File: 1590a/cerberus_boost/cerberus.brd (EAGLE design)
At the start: 33 x 31.7 mm, 30 parts, among them Q1 2N5088, Q2 2N5088, Q3 2N5087

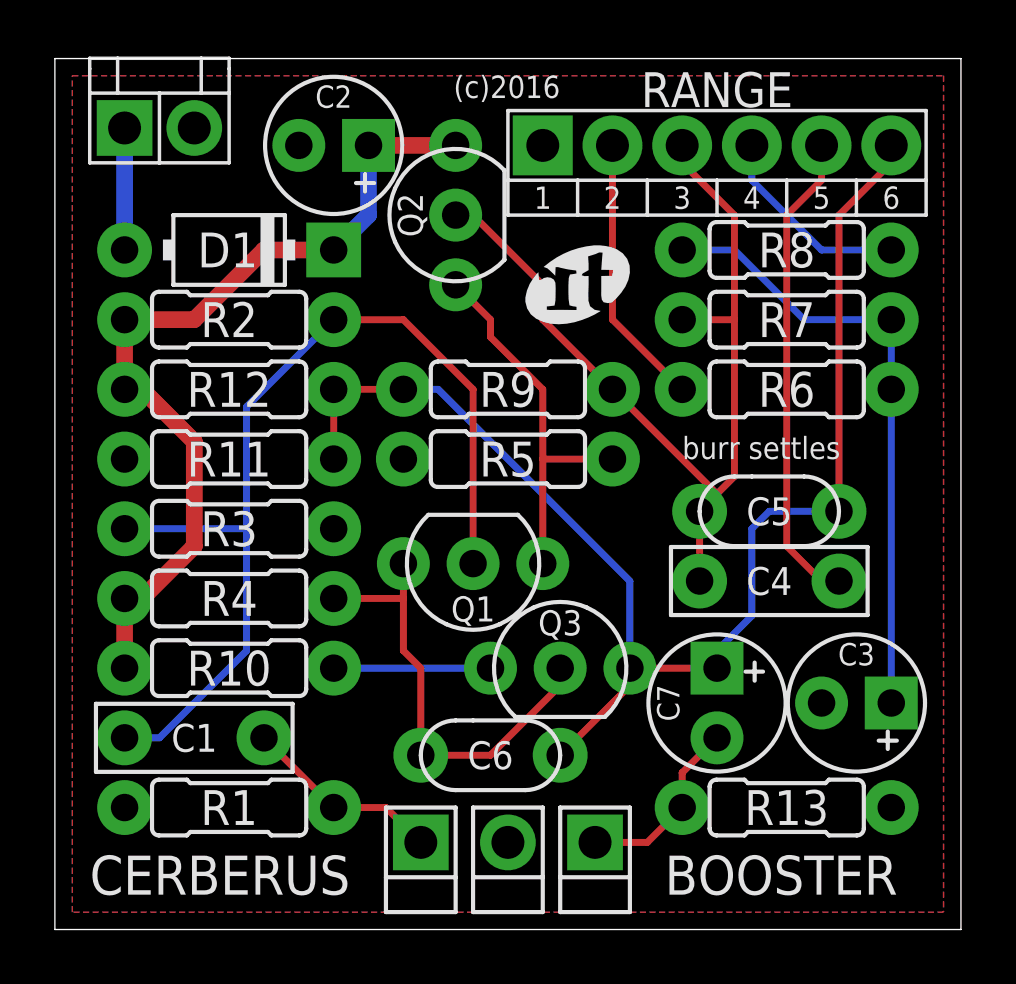
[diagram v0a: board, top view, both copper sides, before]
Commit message: updated library + logos
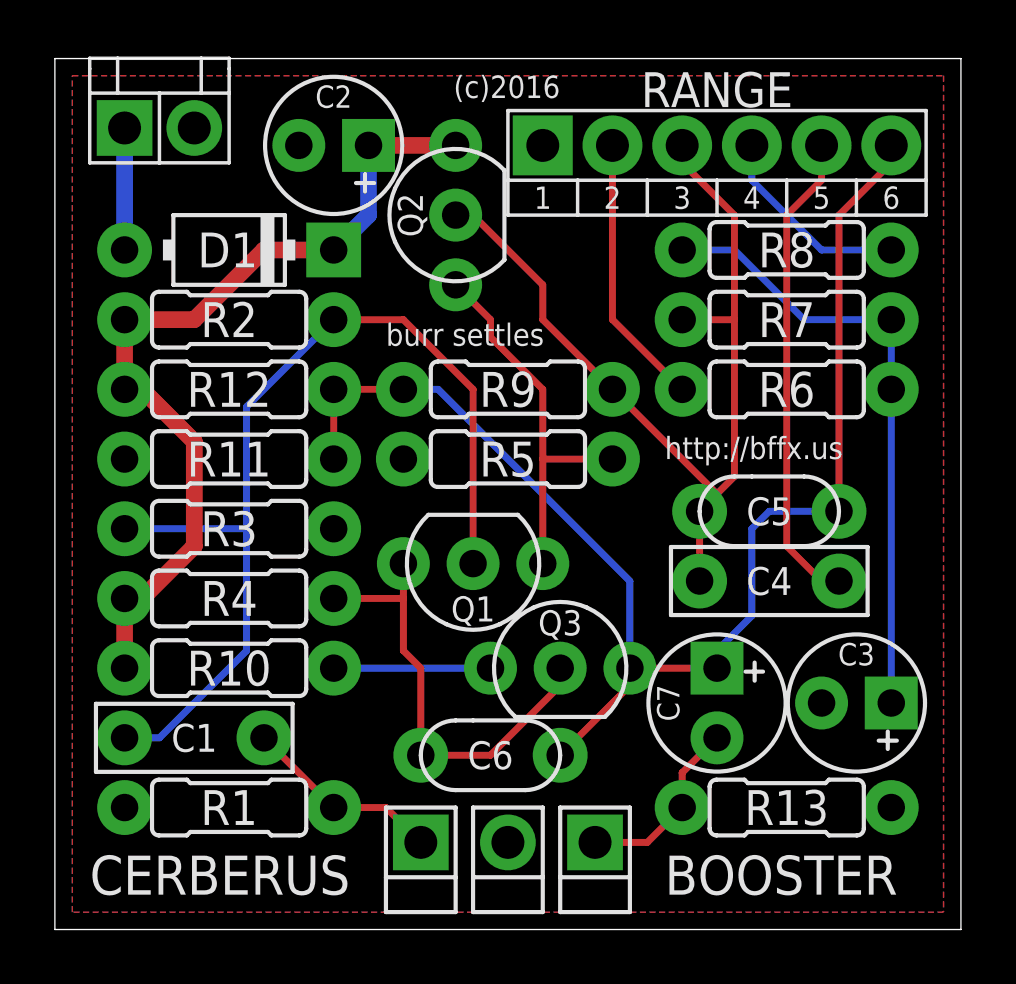
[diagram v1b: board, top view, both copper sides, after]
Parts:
- U$1: device logos:RT0150 -> logos:BF0150
- moved U$1 9.61 mm to (20.3, 14.0)
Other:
- board text added: "http://bffx.us"
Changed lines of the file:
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@@
 <setting verticaltext="up"/>
 </settings>
-<grid distance="25" unitdist="mil" unit="mil" style="lines" multiple="4" display="no" altdistance="0.025" altunitdist="inch" altunit="inch"/>
+<grid distance="12.5" unitdist="mil" unit="mil" style="lines" multiple="4" display="no" altdistance="0.025" altunitdist="inch" altunit="inch"/>
 <layers>
 <layer number="1" name="Top" color="4" fill="1" visible="yes" active="yes"/>
@@
 <text x="22.225" y="1.27" size="1.4224" layer="25" font="vector">BOOSTER</text>
 <text x="18.415" y="31.115" size="0.8128" layer="25" font="vector" rot="R180">(c)2016</text>
-<text x="22.86" y="17.145" size="0.8128" layer="25" font="vector">burr settles</text>
+<text x="12.065" y="21.2725" size="0.8128" layer="25" font="vector">burr settles</text>
+<text x="22.225" y="17.145" size="0.8128" layer="25" font="vector">http://bffx.us</text>
 </plain>
 <attributes>
@@
 <element name="D1" library="diodes" package="DO41-3" value="1N5817" x="6.35" y="24.765" rot="R180"/>
 <element name="9V" library="jacks" package="DC" value="DC_MONO" x="3.81" y="29.21" rot="MR0"/>
-<element name="U$1" library="logos" package="RT0150" value="" x="19.05" y="23.495"/>
+<element name="U$1" library="logos" package="BF0150" value="" x="20.32" y="13.97"/>
 </elements>
 <signals>
